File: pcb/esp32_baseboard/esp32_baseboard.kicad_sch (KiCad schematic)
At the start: 1 part, among them U1 ESP32_DevKit_V1_30Pin

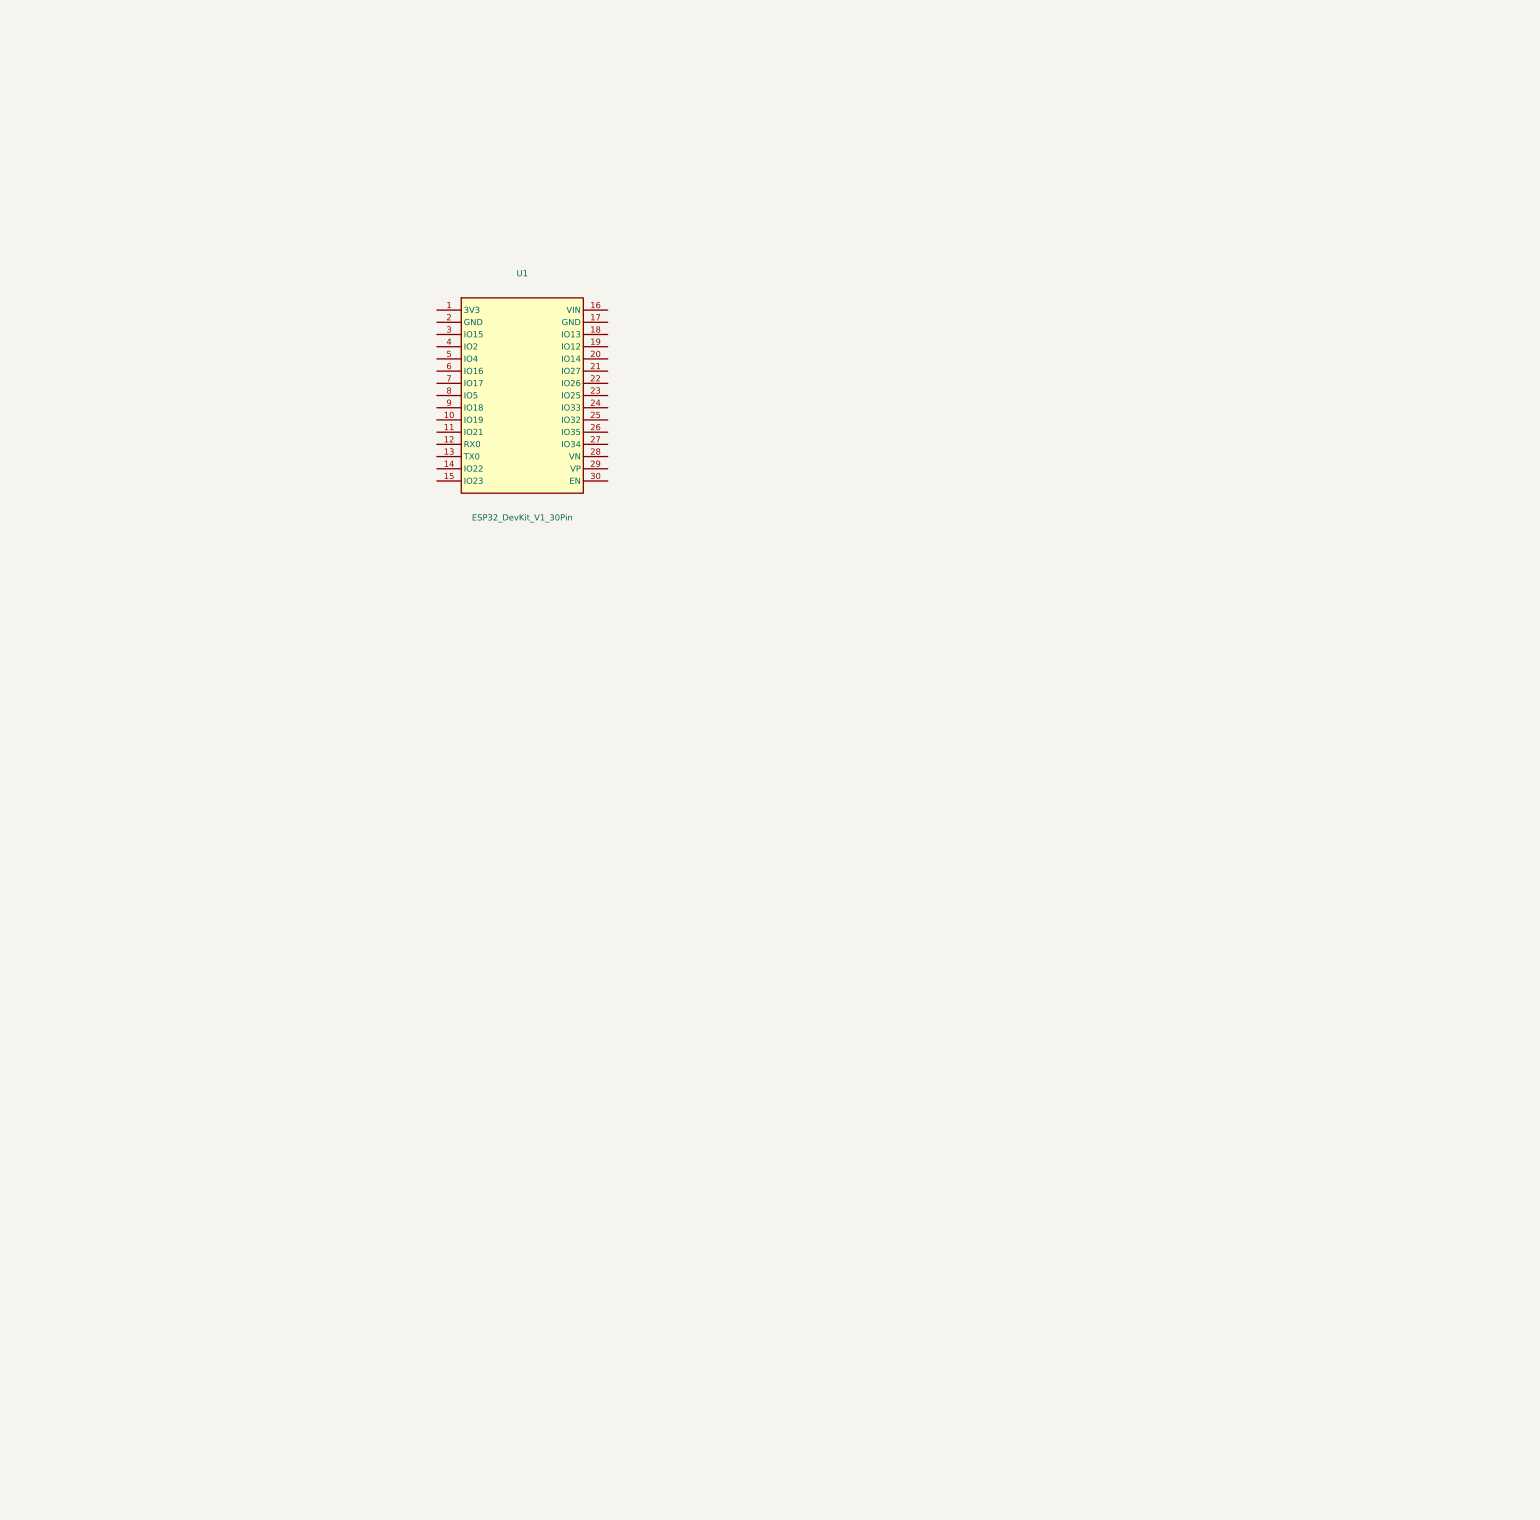
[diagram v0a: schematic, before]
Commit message: tạo PCB mạch base board ghép nối các sub module
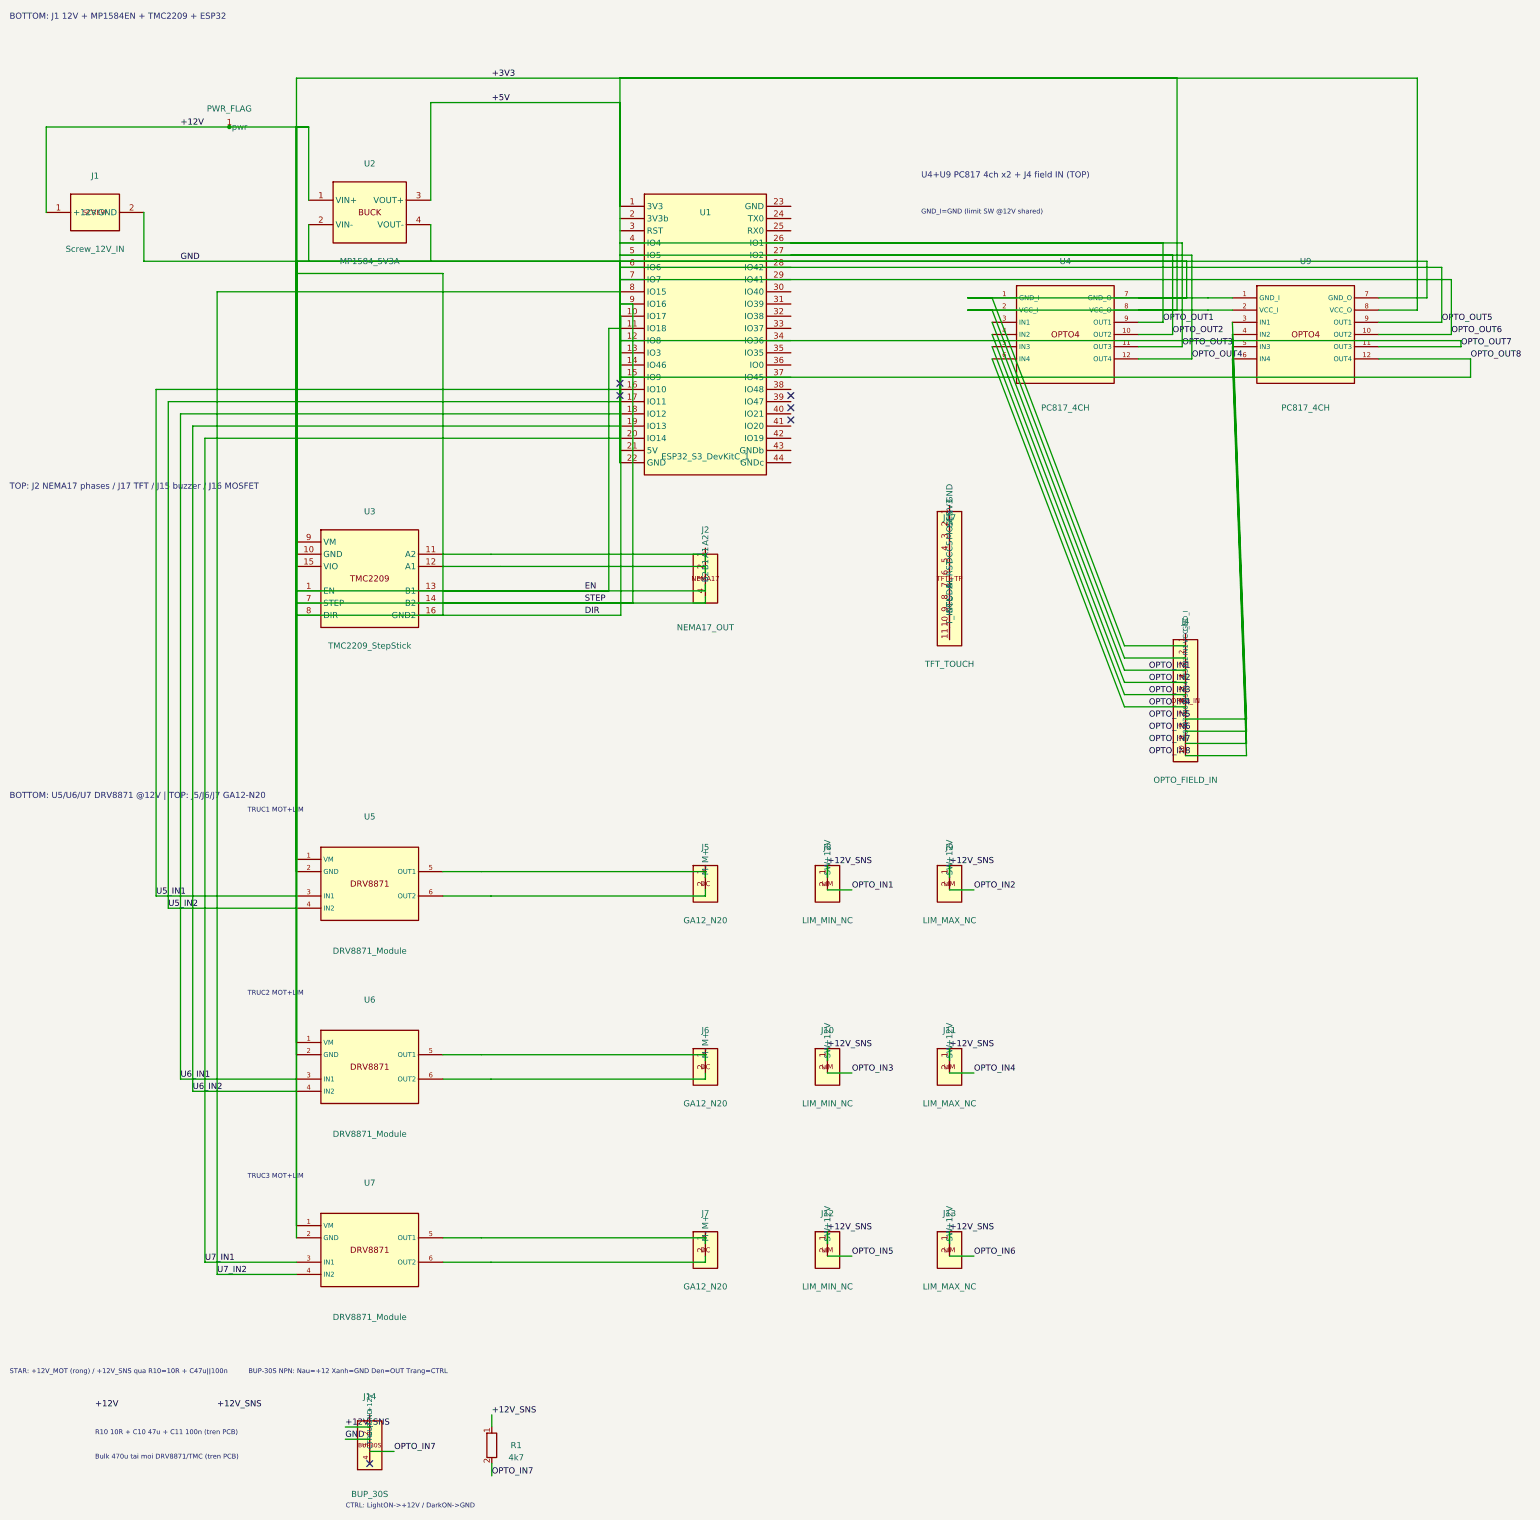
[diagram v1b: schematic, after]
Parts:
- removed U1: ESP32_DevKit_V1_30Pin, ESP32_Carrier:ESP32_DevKit_V1_30Pin_Socket, symbol ESP32_Carrier:ESP32_DevKit_V1_30Pin
- added J1: Screw_12V_IN, ESP32_Carrier:TerminalBlock_2P_5.0mm, symbol ESP32_Carrier:TerminalBlock_2P
- added J10, J12, J8: LIM_MIN_NC, ESP32_Carrier:PinHeader_1x02_LimitSW, symbol ESP32_Carrier:Conn_1x02_LimitSW
- added J11, J13, J9: LIM_MAX_NC, ESP32_Carrier:PinHeader_1x02_LimitSW, symbol ESP32_Carrier:Conn_1x02_LimitSW
- added J14: BUP_30S, ESP32_Carrier:PinHeader_1x04_BUP30S, symbol ESP32_Carrier:Conn_1x04_BUP30S
- added J17: TFT_TOUCH, ESP32_Carrier:PinHeader_1x11_TFT, symbol ESP32_Carrier:Conn_1x11_TFT
- added J2: NEMA17_OUT, ESP32_Carrier:PinHeader_1x04_Motor, symbol ESP32_Carrier:Conn_1x04_Motor
- added J4: OPTO_FIELD_IN, ESP32_Carrier:PinHeader_1x10_OptoField, symbol ESP32_Carrier:Conn_1x10_OptoField
- added J5, J6, J7: GA12_N20, ESP32_Carrier:PinHeader_1x02_MotorDC, symbol ESP32_Carrier:Conn_1x02_MotorDC
- added R1: 4k7, ESP32_Carrier:R_Axial_4k7_BUP, symbol ESP32_Carrier:R_BUP_Pullup
- added U1: ESP32_S3_DevKitC_1, ESP32_Carrier:ESP32_S3_DevKitC_44Pin_Socket, symbol ESP32_Carrier:ESP32_S3_DevKitC_1
- added U2: MP1584_5V3A, ESP32_Carrier:MP1584_5V3A, symbol ESP32_Carrier:MP1584_5V3A
- added U3: TMC2209_StepStick, ESP32_Carrier:TMC2209_StepStick, symbol ESP32_Carrier:TMC2209_StepStick
- added U4, U9: PC817_4CH, ESP32_Carrier:PC817_4CH_Opto, symbol ESP32_Carrier:PC817_4CH_Opto
- added U5, U6, U7: DRV8871_Module, ESP32_Carrier:DRV8871_Module, symbol ESP32_Carrier:DRV8871_Module
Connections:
- new net: J6.1 (M+), U6.5 (OUT1)
- new net: J6.2 (M-), U6.6 (OUT2)
- new net: J5.1 (M+), U5.5 (OUT1)
- new net: J5.2 (M-), U5.6 (OUT2)
- new net: J7.1 (M+), U7.5 (OUT1)
- new net: J7.2 (M-), U7.6 (OUT2)
- new net: J2.1 (A2), U3.11 (A2)
- new net: J2.2 (A1), U3.12 (A1)
- new net: J4.7 (IN5), U9.3 (IN1)
- new net: J4.8 (IN6), U9.4 (IN2)
- new net: J4.9 (IN7), U9.5 (IN3)
- new net: J4.10 (IN8), U9.6 (IN4)
- new net +12V: J1.1 (+12V), J1.2 (GND), J14.2 (GND), J4.1 (GND_I), J4.2 (VCC_I), U1.1 (3V3), U1.21 (5V), U1.22 (GND), U2.1 (VIN+), U2.2 (VIN-), U2.3 (VOUT+), U2.4 (VOUT-), U3.10 (GND), U3.15 (VIO), U3.16 (GND2), U3.9 (VM), U4.1 (GND_I), U4.2 (VCC_I), U4.7 (GND_O), U4.8 (VCC_O), U5.1 (VM), U5.2 (GND), U6.1 (VM), U6.2 (GND), U7.1 (VM), U7.2 (GND), U9.1 (GND_I), U9.2 (VCC_I), U9.7 (GND_O), U9.8 (VCC_O)
- new net +12V_SNS: J10.1 (+12V), J11.1 (+12V), J12.1 (+12V), J13.1 (+12V), J14.1 (+12V), J8.1 (+12V), J9.1 (+12V), R1.1
- new net DIR: U1.10 (IO17), U3.8 (DIR)
- new net EN: J2.3 (B1), U1.11 (IO18), U3.1 (EN), U3.13 (B1)
- new net OPTO_IN1: J4.3 (IN1), J8.2 (SW), U4.3 (IN1)
- new net OPTO_IN2: J4.4 (IN2), J9.2 (SW), U4.4 (IN2)
- new net OPTO_IN3: J10.2 (SW), J4.5 (IN3), U4.5 (IN3)
- new net OPTO_IN4: J11.2 (SW), J4.6 (IN4), U4.6 (IN4)
- new net OPTO_IN5: J12.2 (SW)
- new net OPTO_IN6: J13.2 (SW)
- new net OPTO_IN7: J14.3 (OUT), R1.2
- new net OPTO_OUT1: U1.26 (IO1), U1.4 (IO4), U4.11 (OUT3), U4.9 (OUT1)
- new net OPTO_OUT2: U1.27 (IO2), U1.5 (IO5), U4.10 (OUT2), U4.12 (OUT4)
- new net OPTO_OUT5: U1.6 (IO6), U9.9 (OUT1)
- new net OPTO_OUT6: U1.7 (IO7), U9.10 (OUT2)
- new net OPTO_OUT7: U1.12 (IO8), U9.11 (OUT3)
- new net OPTO_OUT8: U1.15 (IO9), U9.12 (OUT4)
- new net STEP: J2.4 (B2), U1.9 (IO16), U3.14 (B2), U3.7 (STEP)
- new net U5_IN1: U1.16 (IO10), U5.3 (IN1)
- new net U5_IN2: U1.17 (IO11), U5.4 (IN2)
- new net U6_IN1: U1.18 (IO12), U6.3 (IN1)
- new net U6_IN2: U1.19 (IO13), U6.4 (IN2)
- new net U7_IN1: U1.20 (IO14), U7.3 (IN1)
- new net U7_IN2: U1.8 (IO15), U7.4 (IN2)
- no-connect marks 0 -> 6
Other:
- note added: "BOTTOM: J1 12V + MP1584EN + TMC2209 + ESP32"
- note added: "BOTTOM: U5/U6/U7 DRV8871 @12V | TOP: J5/J6/J7 GA12-N20"
- note added: "BUP-30S NPN: Nau=+12 Xanh=GND Den=OUT Trang=CTRL"
- note added: "Bulk 470u tai moi DRV8871/TMC (tren PCB)"
- note added: "CTRL: LightON->+12V / DarkON->GND"
- note added: "GND_I=GND (limit SW @12V shared)"
- note added: "R10 10R + C10 47u + C11 100n (tren PCB)"
- note added: "STAR: +12V_MOT (rong) / +12V_SNS qua R10=10R + C47u||100n"
- note added: "TOP: J2 NEMA17 phases / J17 TFT / J15 buzzer / J16 MOSFET"
- note added: "TRUC1 MOT+LIM"
- note added: "TRUC2 MOT+LIM"
- note added: "TRUC3 MOT+LIM"
- note added: "U4+U9 PC817 4ch x2 + J4 field IN (TOP)"
- title: ESP32 Baseboard -> ESP32-S3 Baseboard - MP1584 + TMC + Opto + 3x DRV8871
